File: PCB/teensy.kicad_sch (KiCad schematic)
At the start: 19 parts, among them Q4 PN2222A, Q5 PN2222A, SW1 PTH_RA_h7.5mm, U2 Teensy4.1, U3 SN74LVC245APW, U5 SN74LVC245APW, U6 SN74LVC245APW, U7 SN74LVC245APW

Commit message: feat: Upload initial PCB v0.3
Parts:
- Q4, Q5: footprint Package_TO_SOT_THT:TO-92_Inline -> Package_TO_SOT_THT:TO-92_Inline_Wide
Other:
- title: ZXTeensyIF1 -> ${PRJ_NAME}
- moved on the sheet: C10, C11, C12, C9, R1

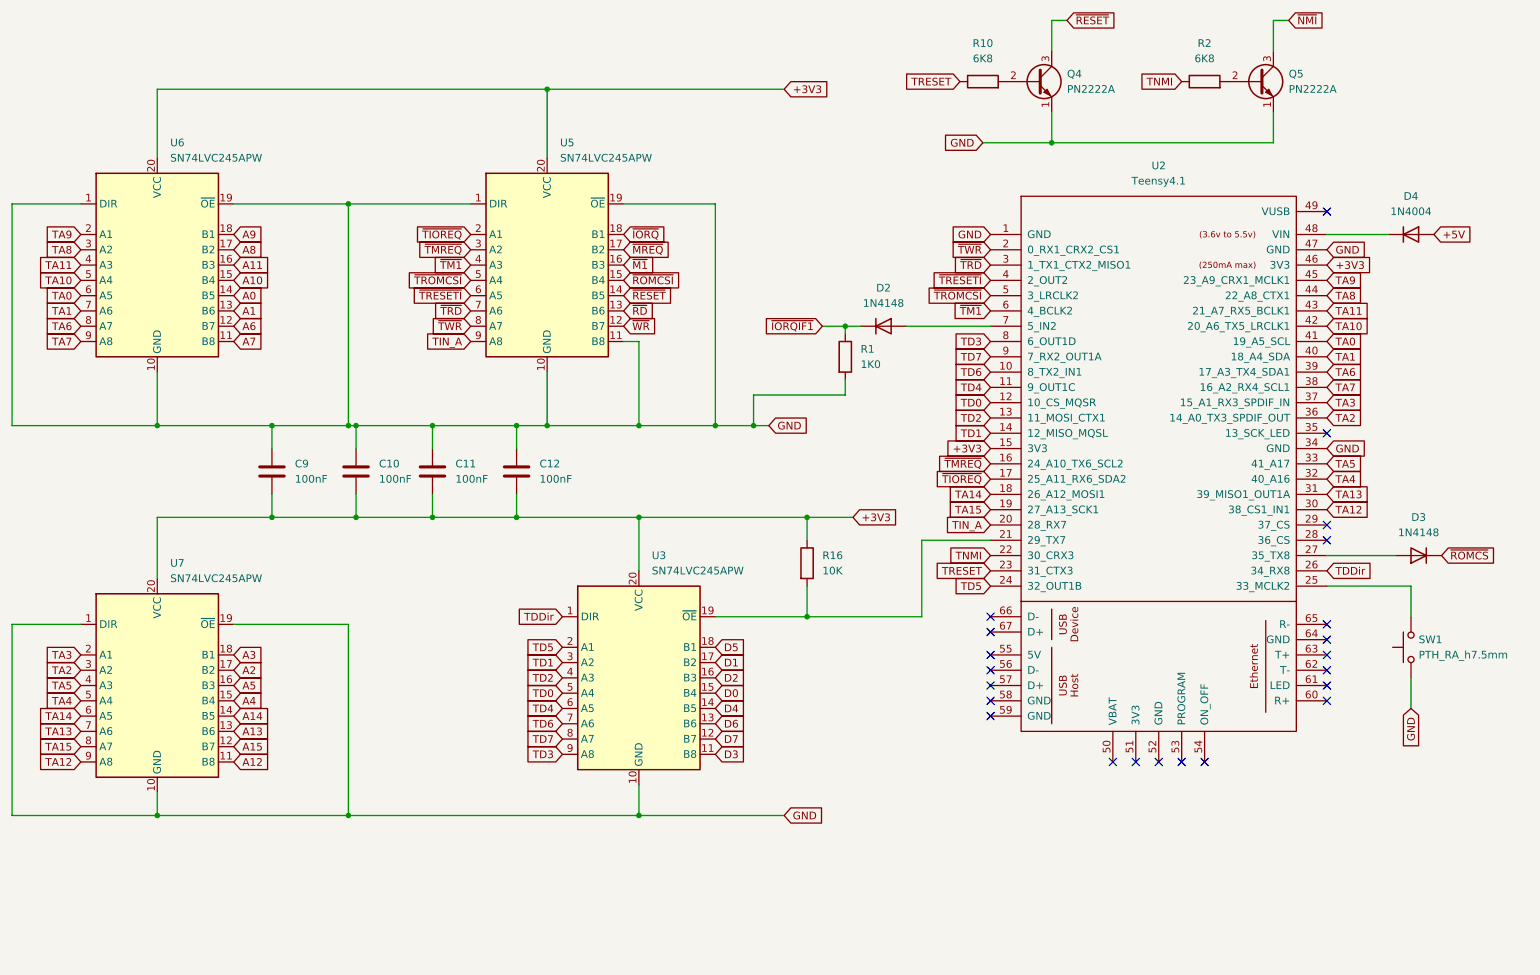
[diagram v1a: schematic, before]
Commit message: feat: Add ESP-01S header to PCB v0.5
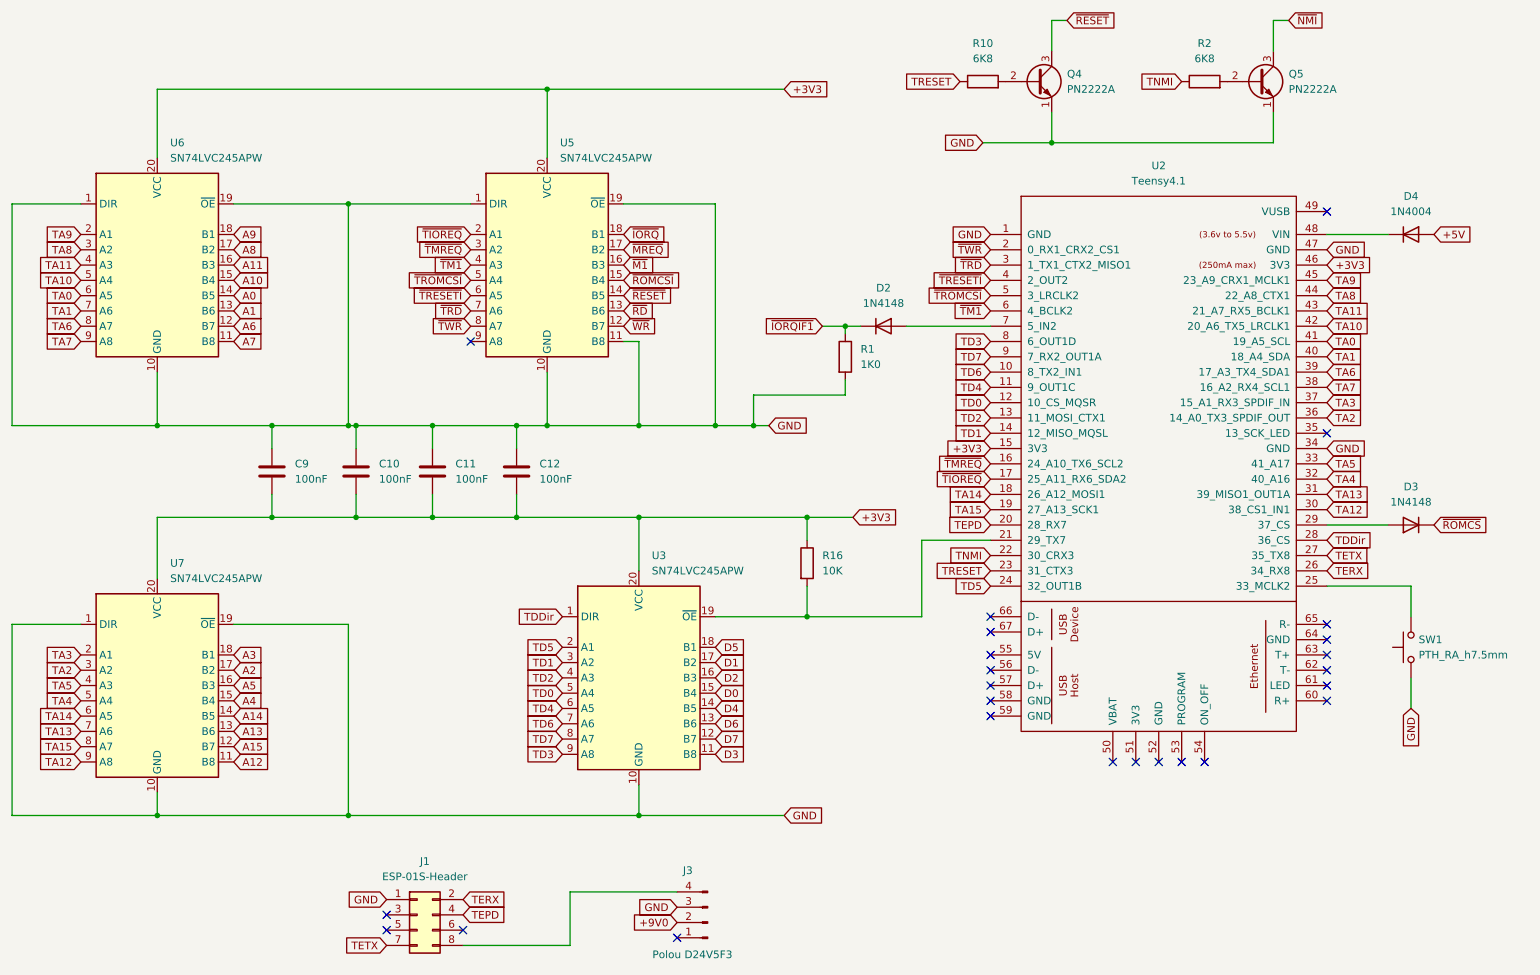
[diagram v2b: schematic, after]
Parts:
- added J1: ESP-01S-Header, Connector_PinSocket_2.54mm:PinSocket_2x04_P2.54mm_Vertical, symbol Connector_Generic:Conn_02x04_Odd_Even
- added J3: Polou D24V5F3, Connector_PinSocket_2.54mm:PinSocket_1x04_P2.54mm_Vertical, symbol Connector:Conn_01x04_Pin
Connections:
- net GND: now also J1.1 (Pin_1), J3.3 (Pin_3)
- net TDDir: now also U2.28 (36_CS); no longer U2.26 (34_RX8)
- net at D3.2 (A): now also U2.29 (37_CS); no longer U2.27 (35_TX8)
- net TIN_A: no longer names the net of U5.9 (A8)
- net TIN_A: no longer U2.20 (28_RX7)
- new net: J1.8 (Pin_8), J3.4 (Pin_4)
- new net +9V0: J3.2 (Pin_2)
- new net TEPD: J1.4 (Pin_4), U2.20 (28_RX7)
- new net TERX: J1.2 (Pin_2), U2.26 (34_RX8)
- new net TETX: J1.7 (Pin_7), U2.27 (35_TX8)
- no-connect marks 22 -> 25
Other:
- moved on the sheet: D3

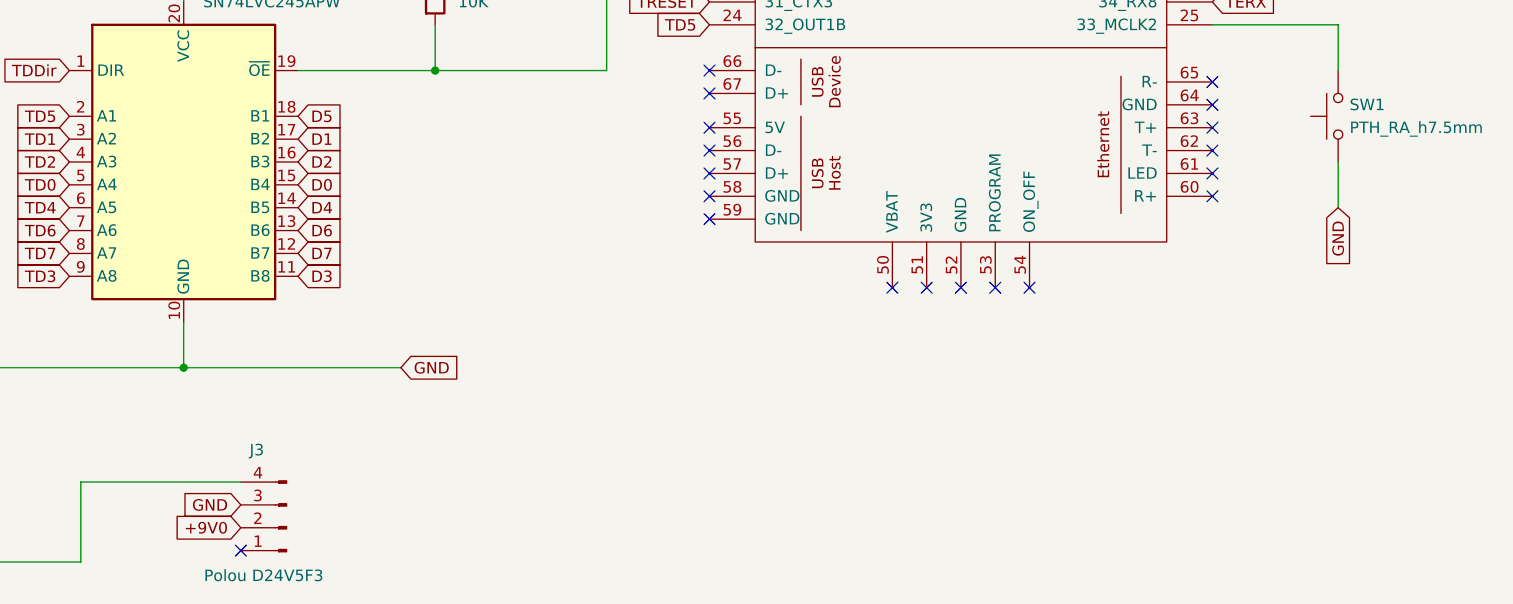
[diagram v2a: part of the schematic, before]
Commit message: Use active DTR and TXDATA from MAX232
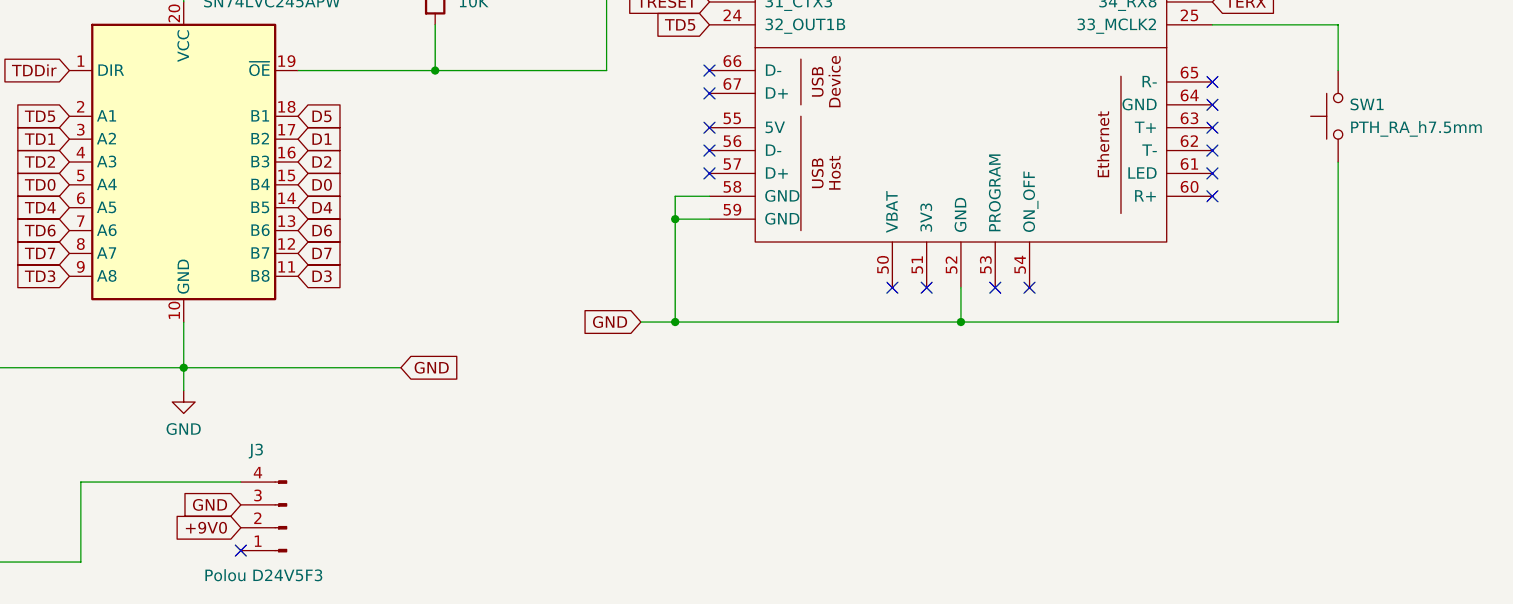
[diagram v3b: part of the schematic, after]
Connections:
- net GND: now also U2.52 (GND), U2.58 (GND), U2.59 (GND)
- no-connect marks 25 -> 22
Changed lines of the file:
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@@
 	)
 	(junction
+		(at 193.04 149.86)
+		(diameter 0)
+		(color 0 0 0 0)
+	)
+	(junction
 		(at 90.17 166.37)
 		(diameter 0)
@@
 	)
 	(junction
+		(at 224.79 161.29)
+		(diameter 0)
+		(color 0 0 0 0)
+	)
+	(junction
 		(at 118.11 116.84)
 		(diameter 0)
@@
 	)
 	(junction
+		(at 193.04 161.29)
+		(diameter 0)
+		(color 0 0 0 0)
+	)
+	(junction
 		(at 207.01 54.61)
 		(diameter 0)
@@
 	)
 	(no_connect
-		(at 224.79 157.48)
-	)
-	(no_connect
 		(at 96.52 182.88)
 	)
@@
 	)
 	(no_connect
-		(at 196.85 149.86)
-	)
-	(no_connect
 		(at 252.73 66.04)
 	)
@@
 	)
 	(no_connect
-		(at 196.85 147.32)
-	)
-	(no_connect
 		(at 228.6 157.48)
 	)
@@
 	(wire
 		(pts
+			(xy 138.43 168.91) (xy 138.43 166.37)
+		)
+		(stroke
+			(width 0)
+			(type default)
+		)
+	)
+	(wire
+		(pts
 			(xy 34.29 134.62) (xy 34.29 166.37)
 		)
@@
 	(wire
 		(pts
+			(xy 193.04 149.86) (xy 196.85 149.86)
+		)
+		(stroke
+			(width 0)
+			(type default)
+		)
+	)
+	(wire
+		(pts
 			(xy 90.17 101.6) (xy 91.44 101.6)
 		)
@@
 	(wire
 		(pts
-			(xy 266.7 143.51) (xy 266.7 148.59)
+			(xy 266.7 143.51) (xy 266.7 161.29)
 		)
 		(stroke
@@
 	(wire
 		(pts
+			(xy 189.23 161.29) (xy 193.04 161.29)
+		)
+		(stroke
+			(width 0)
+			(type default)
+		)
+	)
+	(wire
+		(pts
 			(xy 207.01 39.37) (xy 207.01 34.29)
 		)
@@
 	(wire
 		(pts
+			(xy 196.85 147.32) (xy 193.04 147.32)
+		)
+		(stroke
+			(width 0)
+			(type default)
+		)
+	)
+	(wire
+		(pts
 			(xy 104.14 101.6) (xy 104.14 105.41)
 		)
@@
 	(wire
 		(pts
+			(xy 224.79 157.48) (xy 224.79 161.29)
+		)
+		(stroke
+			(width 0)
+			(type default)
+		)
+	)
+	(wire
+		(pts
+			(xy 193.04 161.29) (xy 224.79 161.29)
+		)
+		(stroke
+			(width 0)
+			(type default)
+		)
+	)
+	(wire
+		(pts
 			(xy 144.78 179.07) (xy 127 179.07)
 		)
@@
 	(wire
 		(pts
+			(xy 193.04 149.86) (xy 193.04 161.29)
+		)
+		(stroke
+			(width 0)
+			(type default)
+		)
+	)
+	(wire
+		(pts
 			(xy 58.42 116.84) (xy 77.47 116.84)
 		)
@@
 	(wire
 		(pts
+			(xy 224.79 161.29) (xy 266.7 161.29)
+		)
+		(stroke
+			(width 0)
+			(type default)
+		)
+	)
+	(wire
+		(pts
 			(xy 91.44 116.84) (xy 104.14 116.84)
 		)
@@
 	(wire
 		(pts
+			(xy 193.04 147.32) (xy 193.04 149.86)
+		)
+		(stroke
+			(width 0)
+			(type default)
+		)
+	)
+	(wire
+		(pts
 			(xy 77.47 113.03) (xy 77.47 116.84)
 		)
@@
 		)
 	)
+	(global_label "GND"
+		(shape input)
+		(at 189.23 161.29 180)
+		(fields_autoplaced yes)
+		(effects
+			(font
+				(size 1.27 1.27)
+			)
+			(justify right)
+		)
+		(property "Intersheetrefs" "${INTERSHEET_REFS}"
+			(at 182.3743 161.29 0)
+			(effects
+				(font
+					(size 1.27 1.27)
+				)
+				(justify right)
+			)
+		)
+	)
 	(global_label "TD2"
 		(shape input)
@@
 		)
 	)
-	(global_label "GND"
-		(shape input)
-		(at 266.7 148.59 270)
-		(fields_autoplaced yes)
-		(effects
-			(font
-				(size 1.27 1.27)
-			)
-			(justify right)
-		)
-		(property "Intersheetrefs" "${INTERSHEET_REFS}"
-			(at 266.7 155.4457 90)
-			(effects
-				(font
-					(size 1.27 1.27)
-				)
-				(justify right)
-			)
-		)
-	)
 	(global_label "~{TRESETI}"
 		(shape input)
@@
 			)
 		)
+	)
+	(symbol
+		(lib_id "power:GND")
+		(at 138.43 168.91 0)
+		(unit 1)
+		(exclude_from_sim no)
+		(in_bom yes)
+		(on_board yes)
+		(dnp no)
+		(fields_autoplaced yes)
+		(property "Reference" "#PWR03"
+			(at 138.43 175.26 0)
+			(effects
+				(font
+					(size 1.27 1.27)
+				)
+				(hide yes)
+			)
+		)
+		(property "Value" "GND"
+			(at 138.43 173.228 0)
+			(effects
+				(font
+					(size 1.27 1.27)
+				)
+			)
+		)
+		(property "Footprint" ""
+			(at 138.43 168.91 0)
+			(effects
+				(font
+					(size 1.27 1.27)
+				)
+				(hide yes)
+			)
+		)
+		(property "Datasheet" ""
+			(at 138.43 168.91 0)
+			(effects
+				(font
+					(size 1.27 1.27)
+				)
+				(hide yes)
+			)
+		)
+		(property "Description" ""
+			(at 138.43 168.91 0)
+			(effects
+				(font
+					(size 1.27 1.27)
+				)
+			)
+		)
+		(pin "1"
+		)
+		(instances
+			(project "ZXTeensyIF1"
+				(path "/75d1cd16-a89a-40a2-b316-dae0403de332/a4045a84-8477-47a3-b33a-d889760d14fe"
+					(reference "#PWR03")
+					(unit 1)
+				)
+			)
+		)
